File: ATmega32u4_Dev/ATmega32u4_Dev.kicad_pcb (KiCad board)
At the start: 4 copper layers, 25.5 x 40.7 mm, 34 parts, among them J1 USB4105-GF-A, J2 ICSP HEader 2x3, J3 Conn_01x14_Pin, J4 Conn_01x14_Pin, SW1 1825910-6, U1 ATmega32U4-A, U2 USBLC6-2SC6, Y1 ABM8-16.000MHZ-10-1-U-T

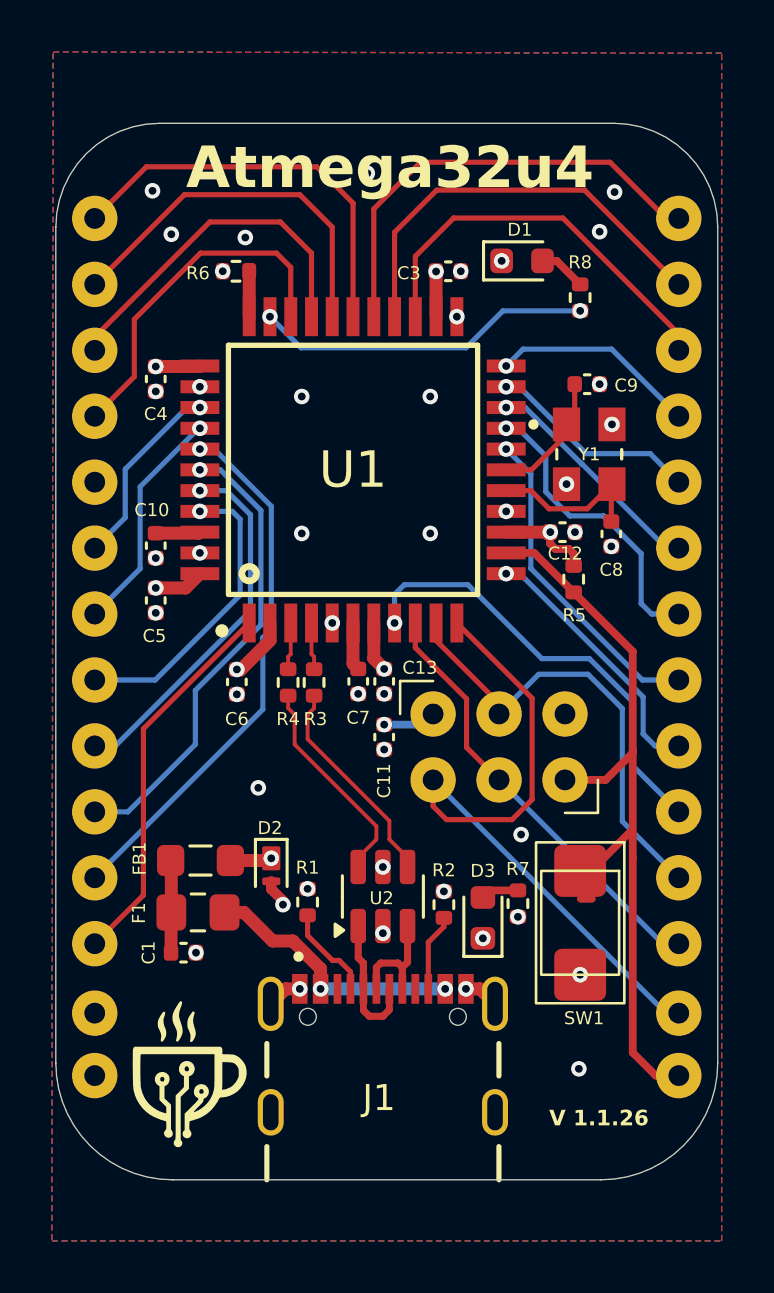
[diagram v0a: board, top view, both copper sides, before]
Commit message: Adjustments to ATmega32, README files, Added SEPIC converter to voltage converters, General progress on other designs
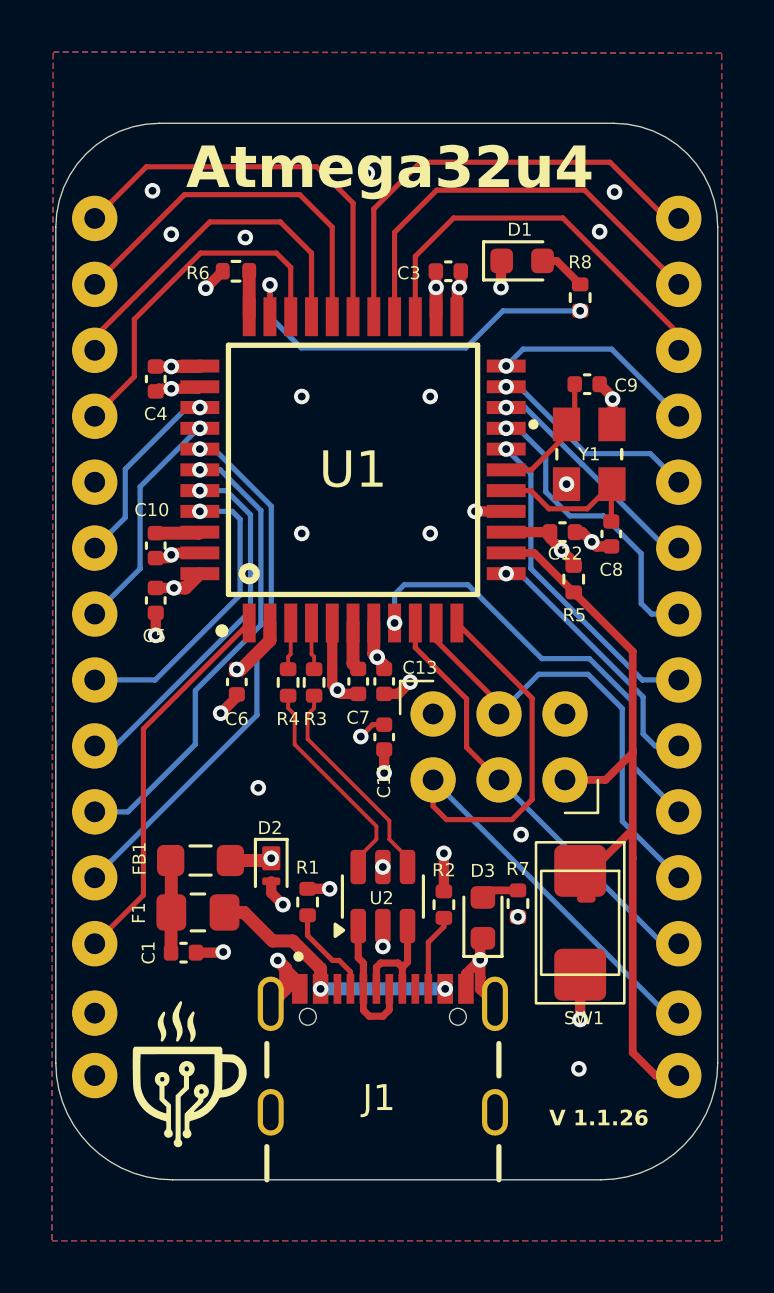
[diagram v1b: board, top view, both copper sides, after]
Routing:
- net GND: track 3.80 -> 33.2 mm, vias 43 -> 36
- net /PC7: track 13.0 -> 15.5 mm
- net MCU_5V: track 17.1 -> 15.8 mm
